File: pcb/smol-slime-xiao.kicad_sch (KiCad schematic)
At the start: 15 parts, among them J1 Battery_Terminal, J2 Charger_Connecter, J3 Conn_01x01, J4 Conn_01x01, SW1 Power_Switch, U1 ICM-45686, U3 1532H, U4 XIAO-nRF52840-SMD

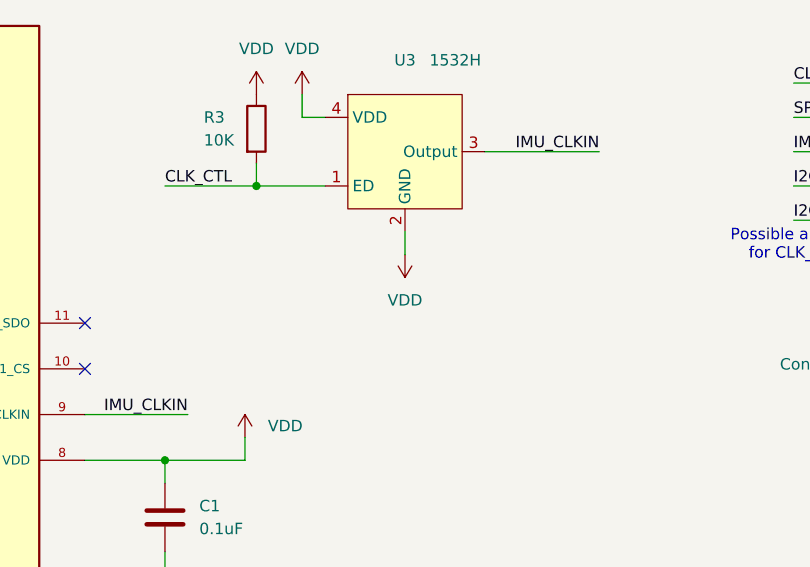
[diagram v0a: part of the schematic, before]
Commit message: Fix mis-wired oscillator
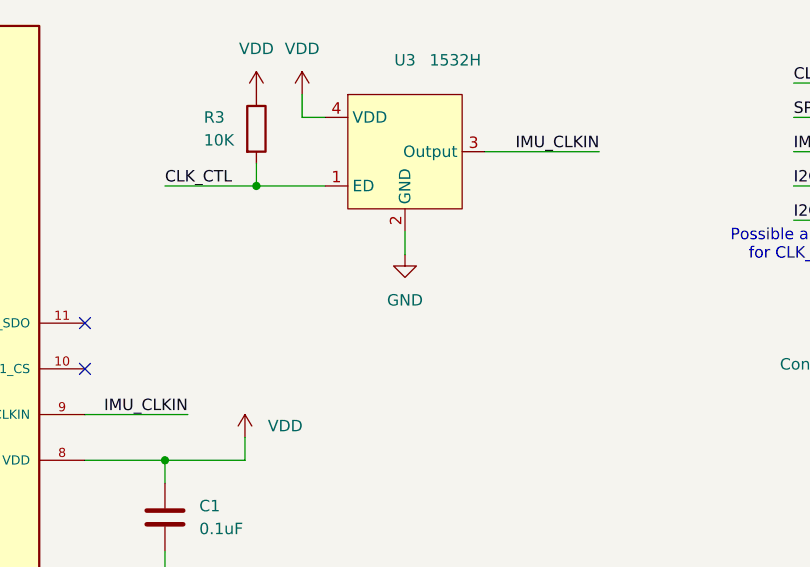
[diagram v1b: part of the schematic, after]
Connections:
- net GND: now also U3.2 (GND)
- net VDD: no longer U3.2 (GND)

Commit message: Fix footprint mismatch
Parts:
- U3: footprint Crystal:Crystal_SMD_3225-4Pin_3.2x2.5mm -> Generic:Crystal_SMD_3225-4Pin_3.2x2.5mm_Silkscreenfix
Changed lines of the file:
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@@
 			)
 		)
-		(property "Footprint" "Crystal:Crystal_SMD_3225-4Pin_3.2x2.5mm"
+		(property "Footprint" "Generic:Crystal_SMD_3225-4Pin_3.2x2.5mm_Silkscreenfix"
 			(at 161.29 52.07 0)
 			(effects

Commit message: Update
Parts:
- J1: JLCPCB Part # (none) -> C295747
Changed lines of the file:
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@@
 			)
 		)
-		(property "Datasheet" "~"
+		(property "Datasheet" "https://jlcpcb.com/partdetail/JST-S2B_PH_SM4_TB_LF_SN/C295747"
 			(at 217.17 82.55 0)
 			(effects
@@
 			(at 217.17 82.55 0)
 			(effects
+				(font
+					(size 1.27 1.27)
+				)
+				(hide yes)
+			)
+		)
+		(property "JLCPCB Part #" "C295747"
+			(at 217.17 82.55 0)
+			(effects

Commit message: Correct part number field name
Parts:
- C1, C2: JLCPCB Part # C1591 -> (none); LCSC PN (none) -> C1591
- C3: JLCPCB Part # C100082 -> (none); LCSC PN (none) -> C100082
- J1: JLCPCB Part # C295747 -> (none); LCSC PN (none) -> C295747
- R1, R2, R3: JLCPCB Part # C15401 -> (none); LCSC PN (none) -> C15401
- SW1: JLCPCB Part # C109335 -> (none); LCSC PN (none) -> C109335
- U1: JLCPCB Part # C22459454 -> (none); LCSC PN (none) -> C22459454
- U2: JLCPCB Part # C5439871 -> (none); LCSC PN (none) -> C5439871
- U3: JLCPCB Part # C5383164 -> (none); LCSC PN (none) -> C5383164
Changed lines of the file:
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@@
 			)
 		)
-		(property "JLCPCB Part #" "C15401"
+		(property "LCSC PN" "C15401"
 			(at 187.96 121.92 0)
 			(effects
@@
 			)
 		)
-		(property "JLCPCB Part #" "C15401"
+		(property "LCSC PN" "C15401"
 			(at 199.39 127 0)
 			(effects
@@
 			)
 		)
-		(property "JLCPCB Part #" "C22459454"
+		(property "LCSC PN" "C22459454"
 			(at 80.01 78.74 0)
 			(effects
@@
 			)
 		)
-		(property "JLCPCB Part #" "C100082"
+		(property "LCSC PN" "C100082"
 			(at 154.94 134.62 0)
 			(effects
@@
 			)
 		)
-		(property "JLCPCB Part #" "C1591"
+		(property "LCSC PN" "C1591"
 			(at 69.85 133.35 0)
 			(effects
@@
 			)
 		)
-		(property "JLCPCB Part #" "C295747"
+		(property "LCSC PN" "C295747"
 			(at 217.17 82.55 0)
 			(effects
@@
 			)
 		)
-		(property "JLCPCB Part #" "C15401"
+		(property "LCSC PN" "C15401"
 			(at 144.78 49.53 0)
 			(effects
@@
 			)
 		)
-		(property "JLCPCB Part #" "C1591"
+		(property "LCSC PN" "C1591"
 			(at 134.62 92.71 0)
 			(effects
@@
 			)
 		)
-		(property "JLCPCB Part #" "C5439871"
+		(property "LCSC PN" "C5439871"
 			(at 172.72 130.81 0)
 			(effects
@@
 			)
 		)
-		(property "JLCPCB Part #" "C5383164"
+		(property "LCSC PN" "C5383164"
 			(at 161.29 52.07 0)
 			(effects
@@
 			)
 		)
-		(property "JLCPCB Part #" "C109335"
+		(property "LCSC PN" "C109335"
 			(at 231.14 91.44 90)
 			(effects

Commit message: Generate BOM and Placement and move gerbers into production dir
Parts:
- J2, J3, J4, U4: now left out of the parts list
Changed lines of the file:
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@@
 		(unit 1)
 		(exclude_from_sim no)
-		(in_bom yes)
-		(on_board yes)
+		(in_bom no)
+		(on_board no)
 		(dnp no)
 		(property "Reference" "J3"
@@
 		(unit 1)
 		(exclude_from_sim no)
-		(in_bom yes)
-		(on_board yes)
+		(in_bom no)
+		(on_board no)
 		(dnp no)
 		(fields_autoplaced yes)
@@
 		(unit 1)
 		(exclude_from_sim no)
-		(in_bom yes)
-		(on_board yes)
+		(in_bom no)
+		(on_board no)
 		(dnp no)
 		(property "Reference" "J4"
@@
 		(unit 1)
 		(exclude_from_sim no)
-		(in_bom yes)
-		(on_board yes)
+		(in_bom no)
+		(on_board no)
 		(dnp no)
 		(property "Reference" "J2"

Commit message: Update oscillator part
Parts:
- U3: LCSC PN C5383164 -> C252344
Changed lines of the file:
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@@
+	(wire
+		(pts
+			(xy 228.6 102.87) (xy 222.25 102.87)
+		)
+		(stroke
+			(width 0)
+			(type default)
+		)
+	)
 	(wire
 		(pts
@@
 	(wire
 		(pts
+			(xy 228.6 96.52) (xy 228.6 102.87)
+		)
+		(stroke
+			(width 0)
+			(type default)
+		)
+	)
+	(wire
+		(pts
 			(xy 241.3 105.41) (xy 222.25 105.41)
 		)
@@
 	(wire
 		(pts
-			(xy 222.25 102.87) (xy 228.6 102.87)
-		)
-		(stroke
-			(width 0)
-			(type default)
-		)
-	)
-	(wire
-		(pts
 			(xy 80.01 124.46) (xy 80.01 139.7)
 		)
@@
 		(pts
 			(xy 233.68 110.49) (xy 233.68 107.95)
-		)
-		(stroke
-			(width 0)
-			(type default)
-		)
-	)
-	(wire
-		(pts
-			(xy 228.6 102.87) (xy 228.6 96.52)
 		)
 		(stroke
@@
 		(exclude_from_sim no)
 		(in_bom no)
-		(on_board no)
+		(on_board yes)
 		(dnp no)
 		(property "Reference" "J3"
@@
 		(exclude_from_sim no)
 		(in_bom no)
-		(on_board no)
+		(on_board yes)
 		(dnp no)
 		(fields_autoplaced yes)
@@
 		(exclude_from_sim no)
 		(in_bom no)
-		(on_board no)
+		(on_board yes)
 		(dnp no)
 		(property "Reference" "J4"
@@
 		(exclude_from_sim no)
 		(in_bom no)
-		(on_board no)
+		(on_board yes)
 		(dnp no)
 		(property "Reference" "J2"
@@
 			)
 		)
-		(property "Datasheet" "https://jlcpcb.com/partdetail/Hci-1532H432K768JWPDTSNL/C5383164"
+		(property "Datasheet" "https://jlcpcb.com/partdetail/247519-3N00032G33YC/C252344"
 			(at 161.29 52.07 0)
 			(effects
@@
 			)
 		)
-		(property "LCSC PN" "C5383164"
+		(property "LCSC PN" "C252344"
 			(at 161.29 52.07 0)
 			(effects

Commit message: Update fro production
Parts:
- J1: now left out of the parts list
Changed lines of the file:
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@@
 		(unit 1)
 		(exclude_from_sim no)
-		(in_bom yes)
+		(in_bom no)
 		(on_board yes)
 		(dnp no)
